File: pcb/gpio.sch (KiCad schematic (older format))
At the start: 1 part, among them U2 A33

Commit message: Finished connecting up the RAM
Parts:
- added unit 4 of U2
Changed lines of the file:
@@
+	1    0    0    -1
+$EndComp
+$Comp
+L Allwinner_A33:A33 U?
+U 4 1 608CB19F
+P 6600 2000
+AR Path="/608CB19F" Ref="U?"  Part="4"
+AR Path="/6063BE69/608CB19F" Ref="U2"  Part="4"
+F 0 "U2" H 7500 2265 50  0000 C CNN
+F 1 "A33" H 7500 2174 50  0000 C CNN
+F 2 "A33_FP:Allwinner_Technology_Co.,_Ltd.-A33-0" H 6600 2400 50  0001 L CNN
+F 3 "http://dl.linux-sunxi.org/A33/A33_Datasheet_release1.0.pdf" H 6600 2500 50  0001 L CNN
+F 4 "1.8V ~ 3.3V" H 6600 2600 50  0001 L CNN "DC Supply Voltage for I/O"
+F 5 "IC" H 6600 2700 50  0001 L CNN "category"
+F 6 "BGA289N80P17X17_1400X1400X129" H 6600 2800 50  0001 L CNN "ipc land pattern name"
+F 7 "yes" H 6600 2900 50  0001 L CNN "lead free"
+F 8 "f6b937119e25c27a" H 6600 3000 50  0001 L CNN "library id"
+F 9 "Allwinner Technology Co., Ltd." H 6600 3100 50  0001 L CNN "manufacturer"
+F 10 "TFBGA282" H 6600 3200 50  0001 L CNN "package"
+F 11 "yes" H 6600 3300 50  0001 L CNN "rohs"
+F 12 "+125°C" H 6600 3400 50  0001 L CNN "temperature range high"
+F 13 "-40°C" H 6600 3500 50  0001 L CNN "temperature range low"
+F 14 "" H 6600 3600 50  0001 L CNN "voltage"
+	4    6600 2000
 	1    0    0    -1
 $EndComp

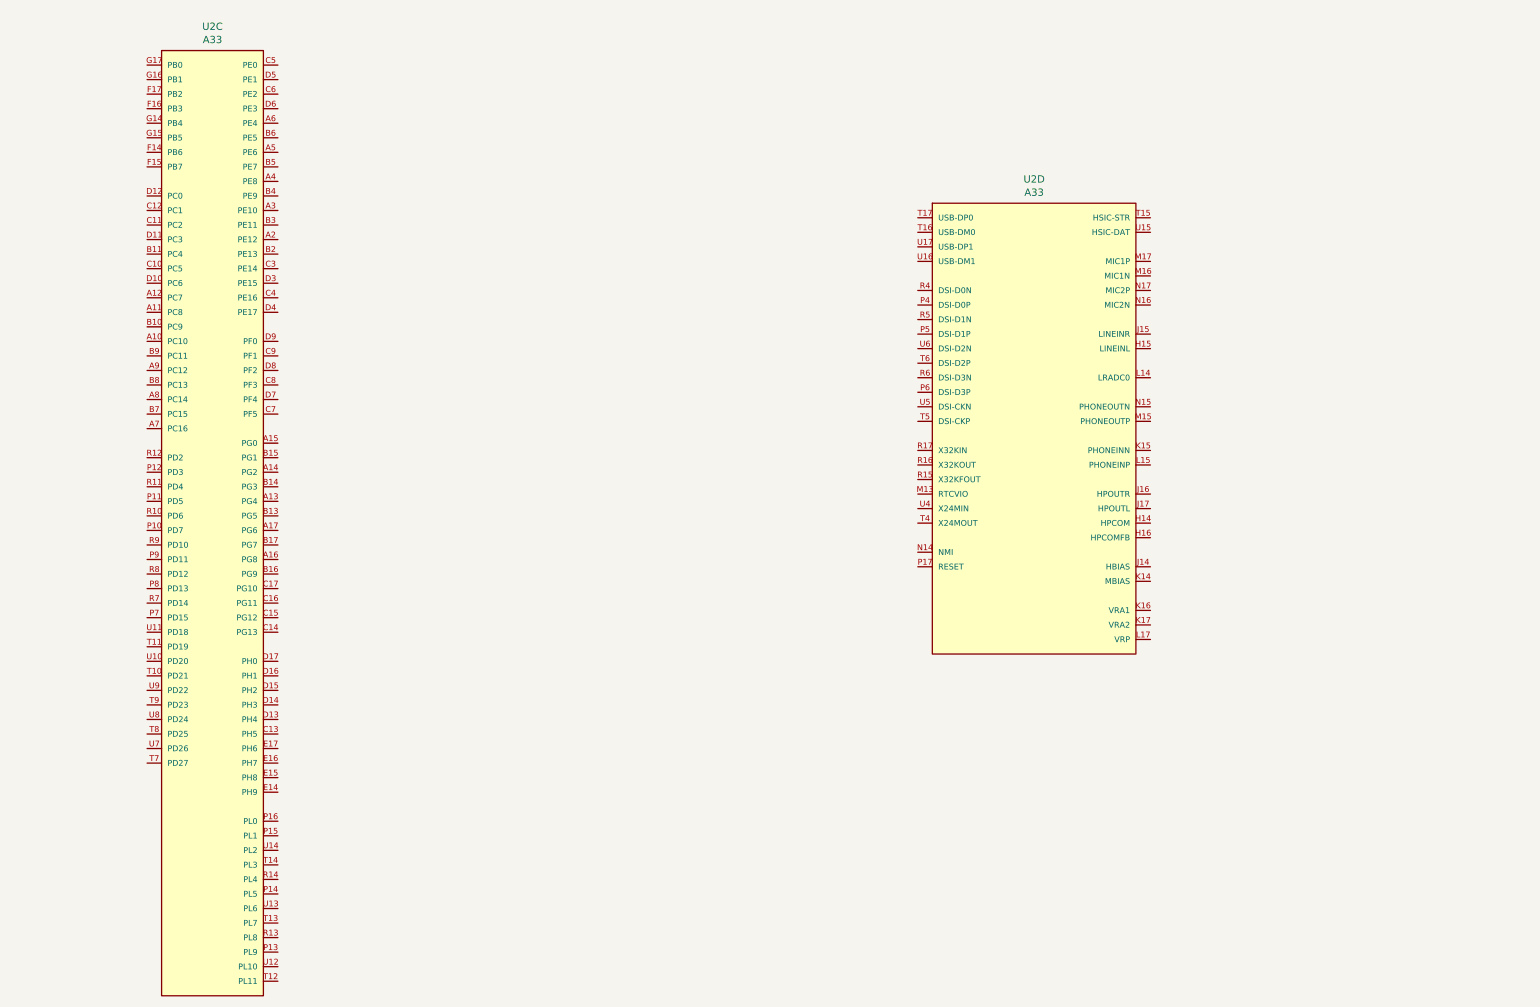
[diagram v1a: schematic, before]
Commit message: Wired in the SD card
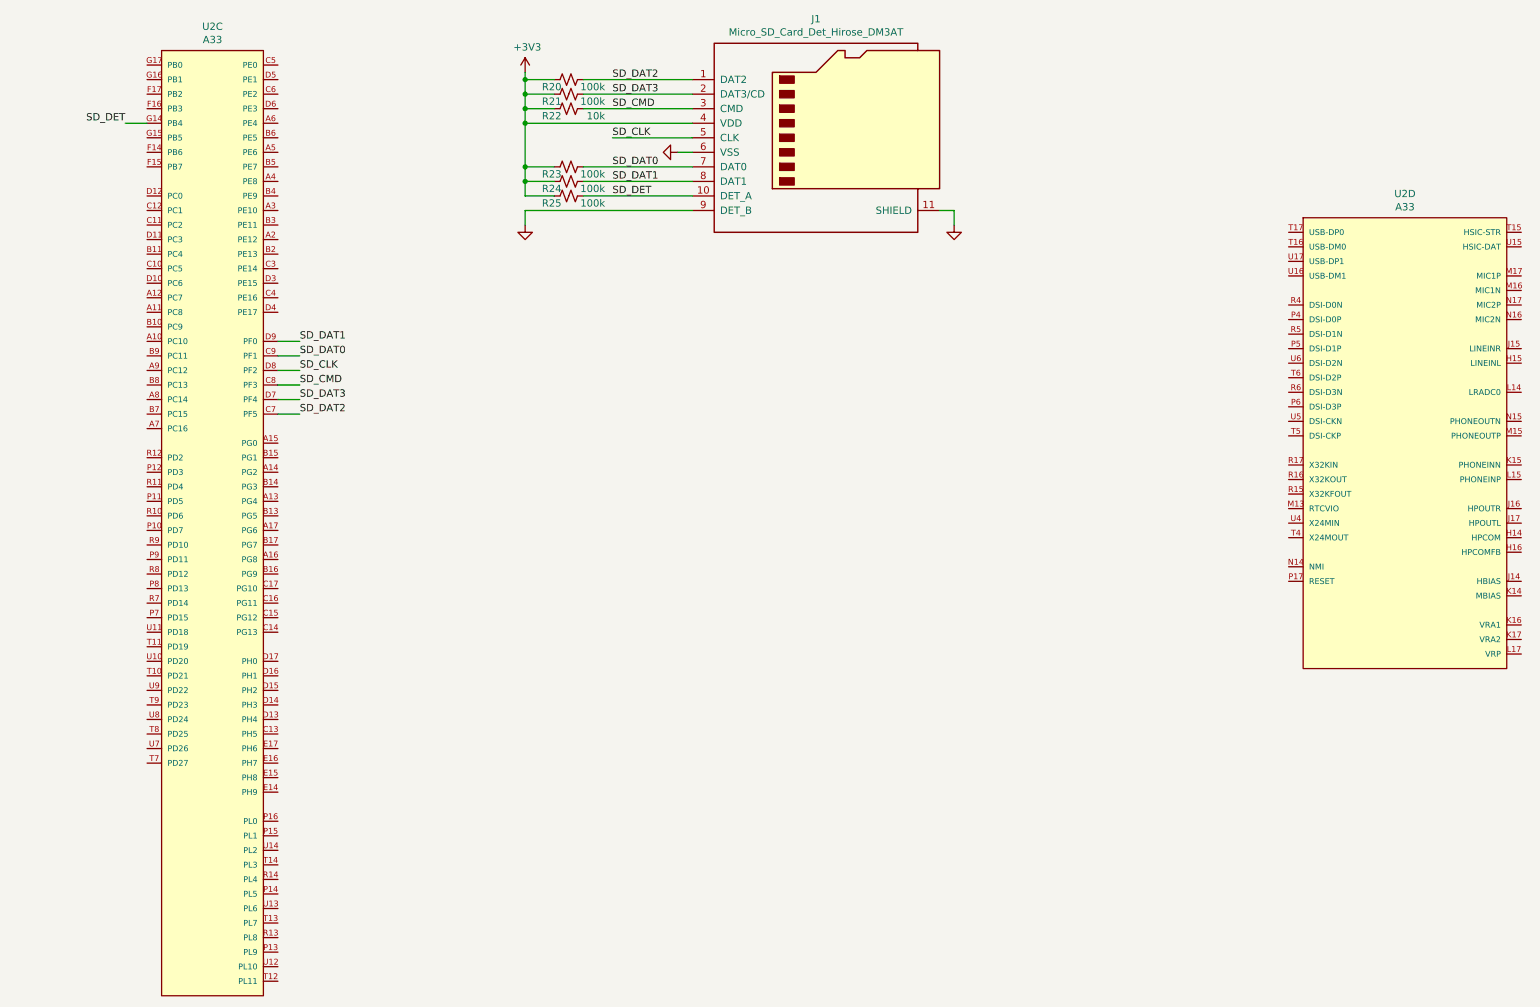
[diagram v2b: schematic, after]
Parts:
- added J1: Micro_SD_Card_Det_Hirose_DM3AT, Connector_Card:microSD_HC_Hirose_DM3AT-SF-PEJM5, symbol Connector:Micro_SD_Card_Det_Hirose_DM3AT
- added R20, R21, R23, R24, R25: 100k, Resistor_SMD:R_0402_1005Metric, symbol Device:R_Small_US
- added R22: 10k, Resistor_SMD:R_0402_1005Metric, symbol Device:R_Small_US
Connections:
- net SD_DAT2: now reaches U2.C7 (PF5)
- net SD_DAT2: now also J1.1 (DAT2), R20.2
- net SD_CMD: now reaches U2.C8 (PF3)
- net SD_CMD: now also J1.3 (CMD), R22.2
- net SD_DAT0: now reaches U2.C9 (PF1)
- net SD_DAT0: now also J1.7 (DAT0), R23.2
- net SD_DAT3: now reaches U2.D7 (PF4)
- net SD_DAT3: now also J1.2 (DAT3/CD), R21.2
- net SD_CLK: now reaches U2.D8 (PF2)
- net SD_CLK: now also J1.5 (CLK)
- net SD_DAT1: now reaches U2.D9 (PF0)
- net SD_DAT1: now also J1.8 (DAT1), R24.2
- net SD_DET: now reaches U2.G14 (PB4)
- net SD_DET: now also J1.10 (DET_A), R25.2
- new net +3V3: J1.4 (VDD), R20.1, R21.1, R22.1, R23.1, R24.1, R25.1
- new net GND: J1.11 (SHIELD), J1.6 (VSS), J1.9 (DET_B)
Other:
- moved on the sheet: U2D

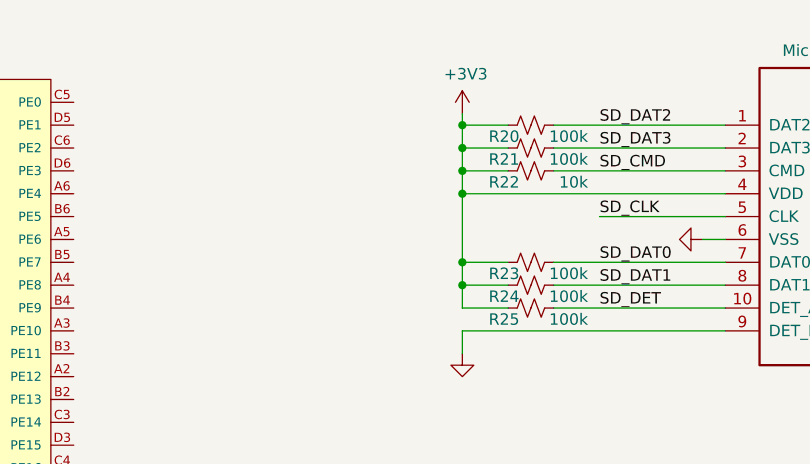
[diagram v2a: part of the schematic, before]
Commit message: Decoupled the SD card.
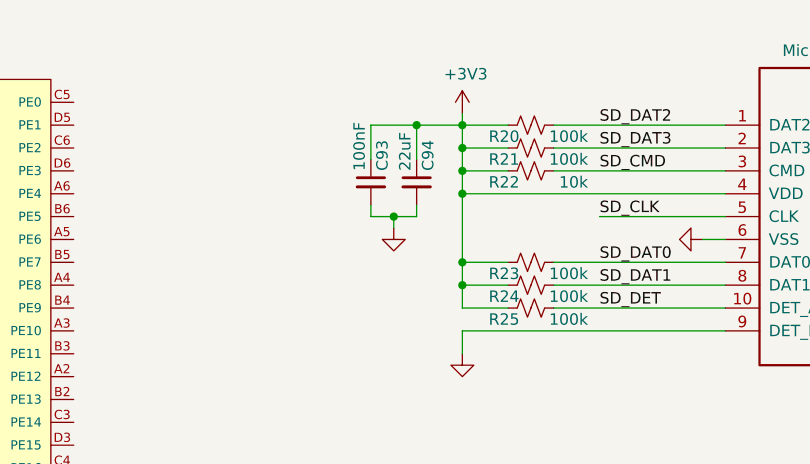
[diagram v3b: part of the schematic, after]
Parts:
- added C93: 100nF, Capacitor_SMD:C_01005_0402Metric, symbol Device:C_Small
- added C94: 22uF, Capacitor_SMD:C_01005_0402Metric, symbol Device:C_Small
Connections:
- net +3V3: now also C93.1, C94.1
- net GND: now also C93.2, C94.2
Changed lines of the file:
@@
 Wire Wire Line
 	1250 1350 1400 1350
+$Comp
+L Device:C_Small C?
+U 1 1 60EE41F9
+P 3600 1300
+AR Path="/60536DA4/60EE41F9" Ref="C?"  Part="1"
+AR Path="/60EE41F9" Ref="C?"  Part="1"
+AR Path="/6063BE69/60EE41F9" Ref="C93"  Part="1"
+F 0 "C93" V 3650 1350 50  0000 L CNN
+F 1 "100nF" V 3550 1350 50  0000 L CNN
+F 2 "Capacitor_SMD:C_01005_0402Metric" H 3600 1300 50  0001 C CNN
+F 3 "~" H 3600 1300 50  0001 C CNN
+	1    3600 1300
+	1    0    0    -1
+$EndComp
+$Comp
+L Device:C_Small C?
+U 1 1 60EE41FF
+P 3800 1300
+AR Path="/60536DA4/60EE41FF" Ref="C?"  Part="1"
+AR Path="/60EE41FF" Ref="C?"  Part="1"
+AR Path="/6063BE69/60EE41FF" Ref="C94"  Part="1"
+F 0 "C94" V 3850 1350 50  0000 L CNN
+F 1 "22uF" V 3750 1350 50  0000 L CNN
+F 2 "Capacitor_SMD:C_01005_0402Metric" H 3800 1300 50  0001 C CNN
+F 3 "~" H 3800 1300 50  0001 C CNN
+	1    3800 1300
+	1    0    0    -1
+$EndComp
+Wire Wire Line
+	3600 1200 3600 1050
+Wire Wire Line
+	3600 1050 3800 1050
+Wire Wire Line
+	3800 1200 3800 1050
+Connection ~ 3800 1050
+Wire Wire Line
+	3800 1050 4000 1050
+Wire Wire Line
+	3800 1400 3800 1450
+Wire Wire Line
+	3800 1450 3700 1450
+Wire Wire Line
+	3600 1450 3600 1400
+$Comp
+L power:GND #PWR?
+U 1 1 60EE9AFE
+P 3700 1500
+AR Path="/60536DA4/60EE9AFE" Ref="#PWR?"  Part="1"
+AR Path="/60EE9AFE" Ref="#PWR?"  Part="1"
+AR Path="/60A30BFF/60EE9AFE" Ref="#PWR?"  Part="1"
+AR Path="/6063BE69/60EE9AFE" Ref="#PWR069"  Part="1"
+F 0 "#PWR069" H 3700 1250 50  0001 C CNN
+F 1 "GND" V 3705 1372 50  0001 R CNN
+F 2 "" H 3700 1500 50  0001 C CNN
+F 3 "" H 3700 1500 50  0001 C CNN
+	1    3700 1500
+	1    0    0    -1
+$EndComp
+Wire Wire Line
+	3700 1500 3700 1450
+Connection ~ 3700 1450
+Wire Wire Line
+	3700 1450 3600 1450
 $EndSCHEMATC

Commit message: Figured out all the crystals
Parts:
- added C95, C96: 10pF, Capacitor_SMD:C_01005_0402Metric, symbol Device:C_Small
- added C97, C98: 30pF, Capacitor_SMD:C_01005_0402Metric, symbol Device:C_Small
- added C99: 10uF, Capacitor_SMD:C_01005_0402Metric, symbol Device:C_Small
- added R29: 10M, Resistor_SMD:R_0402_1005Metric, symbol Device:R_Small_US
- added Y1: 24Mhz, Crystal:Crystal_SMD_Abracon_ABM8G-4Pin_3.2x2.5mm, symbol Device:Crystal_GND24_Small
- added Y2: 32.768khz, Abracon:Abracon-ABS05-0-0-MFG, symbol Device:Crystal_Small
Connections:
- net GND: now also C95.1, C96.1, C97.2, C98.2, C99.2, Y1.2, Y1.4
- net at U2.M13 (RTCVIO): now also C99.1
- net at U2.R16 (X32KOUT): now also C96.2, R29.2, Y2.2
- net at U2.R17 (X32KIN): now also C95.2, R29.1, Y2.1
- net at U2.T4 (X24MOUT): now also C98.1, Y1.1
- net at U2.U4 (X24MIN): now also C97.1, Y1.3
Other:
- moved on the sheet: U2D

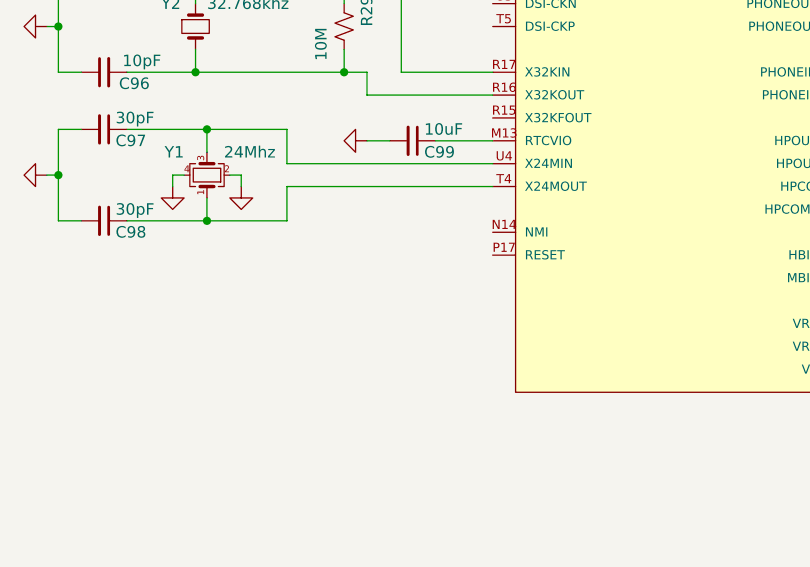
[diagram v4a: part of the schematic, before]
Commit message: Wired in the NMI and reset pins.
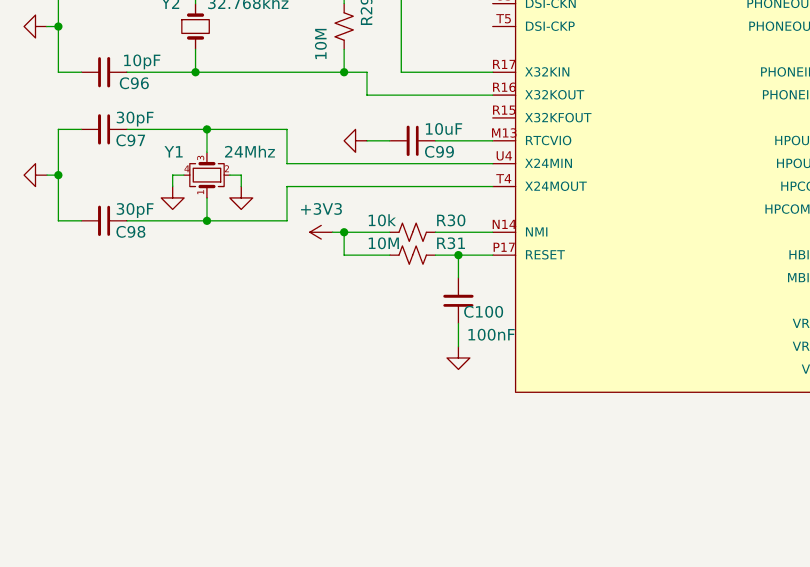
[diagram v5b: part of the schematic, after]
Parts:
- added C100: 100nF, Capacitor_SMD:C_01005_0402Metric, symbol Device:C_Small
- added R30: 10k, Resistor_SMD:R_0402_1005Metric, symbol Device:R_Small_US
- added R31: 10M, Resistor_SMD:R_0402_1005Metric, symbol Device:R_Small_US
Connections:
- net +3V3: now also R30.2, R31.2
- net GND: now also C100.1
- net at U2.N14 (NMI): now also R30.1
- net at U2.P17 (RESET): now also C100.2, R31.1
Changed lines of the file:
@@
 	0    1    1    0
 $EndComp
+Wire Wire Line
+	8050 5300 7800 5300
+$Comp
+L power:+3V3 #PWR?
+U 1 1 606D2633
+P 7350 5300
+AR Path="/60A30BFF/606D2633" Ref="#PWR?"  Part="1"
+AR Path="/606D2633" Ref="#PWR?"  Part="1"
+AR Path="/6063BE69/606D2633" Ref="#PWR075"  Part="1"
+F 0 "#PWR075" H 7350 5150 50  0001 C CNN
+F 1 "+3V3" V 7450 5350 50  0000 C CNN
+F 2 "" H 7350 5300 50  0001 C CNN
+F 3 "" H 7350 5300 50  0001 C CNN
+	1    7350 5300
+	0    -1   -1   0
+$EndComp
+$Comp
+L Device:R_Small_US R?
+U 1 1 606E17EE
+P 7700 5300
+AR Path="/60536DA4/606E17EE" Ref="R?"  Part="1"
+AR Path="/606E17EE" Ref="R?"  Part="1"
+AR Path="/6063BE69/606E17EE" Ref="R30"  Part="1"
+F 0 "R30" V 7650 5400 50  0000 L CNN
+F 1 "10k" V 7650 5100 50  0000 L CNN
+F 2 "Resistor_SMD:R_0402_1005Metric" H 7700 5300 50  0001 C CNN
+F 3 "~" H 7700 5300 50  0001 C CNN
+	1    7700 5300
+	0    1    1    0
+$EndComp
+Wire Wire Line
+	7600 5300 7400 5300
+Wire Wire Line
+	7400 5300 7400 5400
+Wire Wire Line
+	7400 5400 7600 5400
+Connection ~ 7400 5300
+Wire Wire Line
+	7400 5300 7350 5300
+$Comp
+L Device:R_Small_US R?
+U 1 1 606E6005
+P 7700 5400
+AR Path="/60536DA4/606E6005" Ref="R?"  Part="1"
+AR Path="/606E6005" Ref="R?"  Part="1"
+AR Path="/6063BE69/606E6005" Ref="R31"  Part="1"
+F 0 "R31" V 7650 5500 50  0000 L CNN
+F 1 "10M" V 7650 5200 50  0000 L CNN
+F 2 "Resistor_SMD:R_0402_1005Metric" H 7700 5400 50  0001 C CNN
+F 3 "~" H 7700 5400 50  0001 C CNN
+	1    7700 5400
+	0    1    1    0
+$EndComp
+Wire Wire Line
+	7800 5400 7900 5400
+$Comp
+L Device:C_Small C?
+U 1 1 606FB519
+P 7900 5600
+AR Path="/60536DA4/606FB519" Ref="C?"  Part="1"
+AR Path="/606FB519" Ref="C?"  Part="1"
+AR Path="/6063BE69/606FB519" Ref="C100"  Part="1"
+F 0 "C100" H 7700 5650 50  0000 L CNN
+F 1 "100nF" H 7650 5750 50  0000 L CNN
+F 2 "Capacitor_SMD:C_01005_0402Metric" H 7900 5600 50  0001 C CNN
+F 3 "~" H 7900 5600 50  0001 C CNN
+	1    7900 5600
+	-1   0    0    1
+$EndComp
+Wire Wire Line
+	7900 5500 7900 5400
+$Comp
+L power:GND #PWR?
+U 1 1 606FF627
+P 7900 5800
+AR Path="/60536DA4/606FF627" Ref="#PWR?"  Part="1"
+AR Path="/606FF627" Ref="#PWR?"  Part="1"
+AR Path="/60A30BFF/606FF627" Ref="#PWR?"  Part="1"
+AR Path="/6063BE69/606FF627" Ref="#PWR076"  Part="1"
+F 0 "#PWR076" H 7900 5550 50  0001 C CNN
+F 1 "GND" V 7905 5672 50  0001 R CNN
+F 2 "" H 7900 5800 50  0001 C CNN
+F 3 "" H 7900 5800 50  0001 C CNN
+	1    7900 5800
+	1    0    0    -1
+$EndComp
+Wire Wire Line
+	7900 5800 7900 5700
+Connection ~ 7900 5400
+Wire Wire Line
+	7900 5400 8050 5400
 $EndSCHEMATC
